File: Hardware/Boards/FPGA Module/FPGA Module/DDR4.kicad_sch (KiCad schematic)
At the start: 39 parts, among them U17 MT40A512M16LY-075:E, U9 TPS74801AWDRC

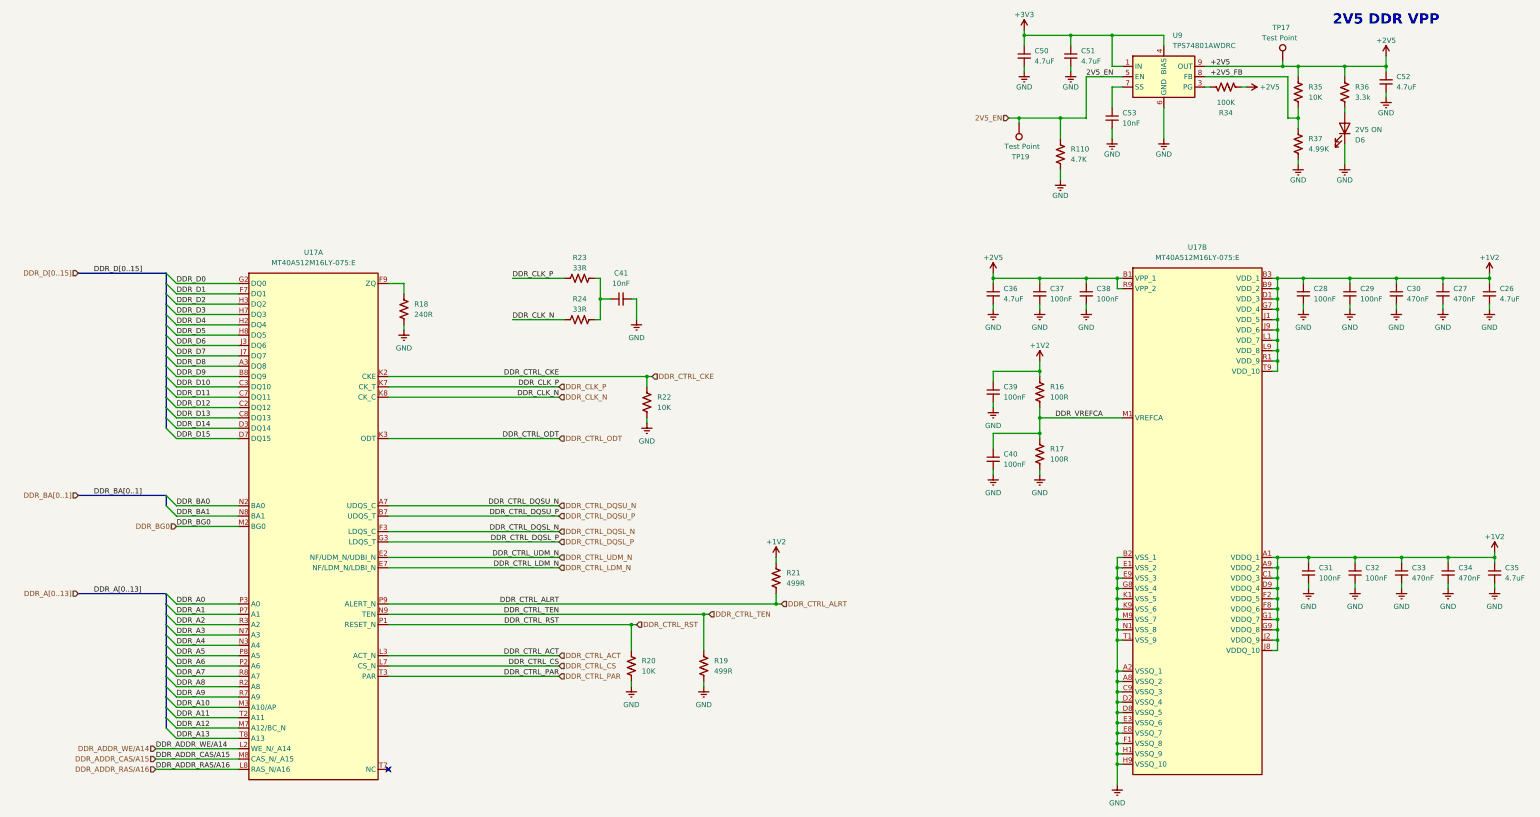
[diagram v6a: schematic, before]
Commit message: Completed FPGA module PCB layout
Started PCB routing
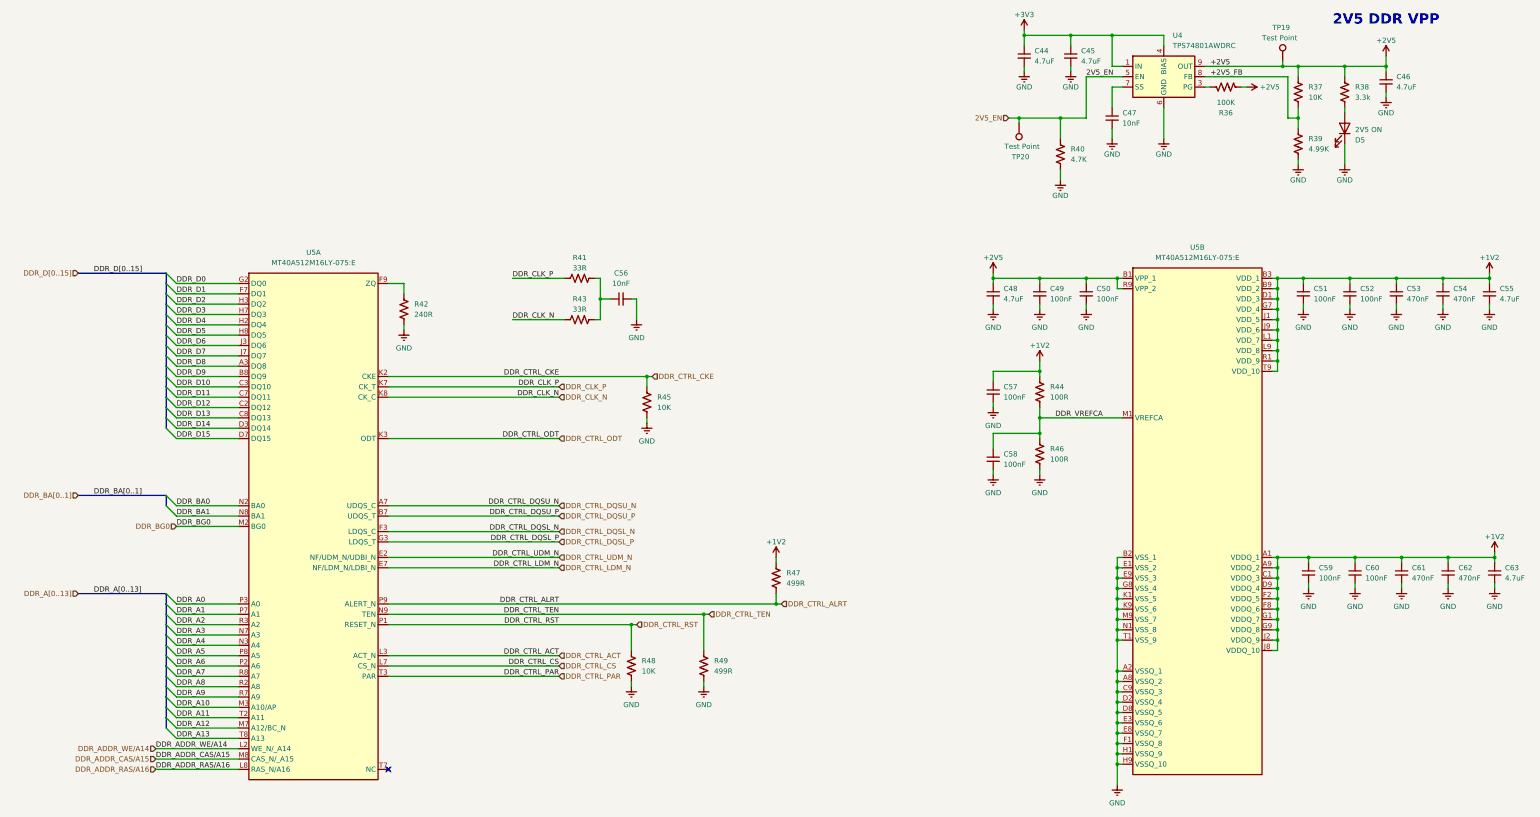
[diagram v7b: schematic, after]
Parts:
- C47: renamed from C53; footprint Capacitor_SMD:C_0402_1005Metric -> Capacitor_SMD:C_0201_0603Metric
- C49: renamed from C37; footprint Capacitor_SMD:C_0402_1005Metric -> Capacitor_SMD:C_0201_0603Metric
- C50: renamed from C38; footprint Capacitor_SMD:C_0402_1005Metric -> Capacitor_SMD:C_0201_0603Metric
- C51: renamed from C28; footprint Capacitor_SMD:C_0402_1005Metric -> Capacitor_SMD:C_0201_0603Metric
- C52: renamed from C29; footprint Capacitor_SMD:C_0402_1005Metric -> Capacitor_SMD:C_0201_0603Metric
- C53: renamed from C30; footprint Capacitor_SMD:C_0402_1005Metric -> Capacitor_SMD:C_0201_0603Metric
- C54: renamed from C27; footprint Capacitor_SMD:C_0402_1005Metric -> Capacitor_SMD:C_0201_0603Metric
- C56: renamed from C41; footprint Capacitor_SMD:C_0402_1005Metric -> Capacitor_SMD:C_0201_0603Metric
- C57: renamed from C39; footprint Capacitor_SMD:C_0402_1005Metric -> Capacitor_SMD:C_0201_0603Metric
- C58: renamed from C40; footprint Capacitor_SMD:C_0402_1005Metric -> Capacitor_SMD:C_0201_0603Metric
- C59: renamed from C31; footprint Capacitor_SMD:C_0402_1005Metric -> Capacitor_SMD:C_0201_0603Metric
- C60: renamed from C32; footprint Capacitor_SMD:C_0402_1005Metric -> Capacitor_SMD:C_0201_0603Metric
- C61: renamed from C33; footprint Capacitor_SMD:C_0402_1005Metric -> Capacitor_SMD:C_0201_0603Metric
- C62: renamed from C34; footprint Capacitor_SMD:C_0402_1005Metric -> Capacitor_SMD:C_0201_0603Metric
- R36: renamed from R34; footprint Resistor_SMD:R_0402_1005Metric -> Resistor_SMD:R_0201_0603Metric
- R37: renamed from R35; footprint Resistor_SMD:R_0402_1005Metric -> Resistor_SMD:R_0201_0603Metric
- R38: renamed from R36; footprint Resistor_SMD:R_0402_1005Metric -> Resistor_SMD:R_0201_0603Metric
- R39: renamed from R37; footprint Resistor_SMD:R_0402_1005Metric -> Resistor_SMD:R_0201_0603Metric
- R40: renamed from R110; footprint Resistor_SMD:R_0402_1005Metric -> Resistor_SMD:R_0201_0603Metric
- R41: renamed from R23; footprint Resistor_SMD:R_0402_1005Metric -> Resistor_SMD:R_0201_0603Metric
- R42: renamed from R18; footprint Resistor_SMD:R_0402_1005Metric -> Resistor_SMD:R_0201_0603Metric
- R43: renamed from R24; footprint Resistor_SMD:R_0402_1005Metric -> Resistor_SMD:R_0201_0603Metric
- R44: renamed from R16; footprint Resistor_SMD:R_0402_1005Metric -> Resistor_SMD:R_0201_0603Metric
- R45: renamed from R22; footprint Resistor_SMD:R_0402_1005Metric -> Resistor_SMD:R_0201_0603Metric
- R46: renamed from R17; footprint Resistor_SMD:R_0402_1005Metric -> Resistor_SMD:R_0201_0603Metric
- R47: renamed from R21; footprint Resistor_SMD:R_0402_1005Metric -> Resistor_SMD:R_0201_0603Metric
- R48: renamed from R20; footprint Resistor_SMD:R_0402_1005Metric -> Resistor_SMD:R_0201_0603Metric
- R49: renamed from R19; footprint Resistor_SMD:R_0402_1005Metric -> Resistor_SMD:R_0201_0603Metric
- renumbered C50 to C44, C51 to C45, C52 to C46, C36 to C48, C26 to C55, C35 to C63, D6 to D5, TP17 to TP19, TP19 to TP20, U9 to U4, U17 to U5

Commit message: Updated SCH and Layout
Added temp sensors for DCDC's, Added MCU control for FPGA mode, removed mode DIP switch
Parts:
- C44, C45, C46, C48, C55, C63: footprint Capacitor_SMD:C_0402_1005Metric -> Capacitor_SMD:C_0201_0603Metric
- R39: value 4.99K -> 5.1K
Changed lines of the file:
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@@
 			)
 		)
-		(property "Footprint" "Capacitor_SMD:C_0402_1005Metric"
+		(property "Footprint" "Capacitor_SMD:C_0201_0603Metric"
 			(at 270.51 38.1 0)
 			(effects
@@
 			)
 		)
-		(property "Footprint" "Capacitor_SMD:C_0402_1005Metric"
+		(property "Footprint" "Capacitor_SMD:C_0201_0603Metric"
 			(at 386.08 165.1 0)
 			(effects
@@
 			)
 		)
-		(property "Footprint" "Capacitor_SMD:C_0402_1005Metric"
+		(property "Footprint" "Capacitor_SMD:C_0201_0603Metric"
 			(at 359.41 44.45 0)
 			(effects
@@
 			)
 		)
-		(property "Footprint" "Capacitor_SMD:C_0402_1005Metric"
+		(property "Footprint" "Capacitor_SMD:C_0201_0603Metric"
 			(at 262.89 96.52 0)
 			(effects
@@
 			)
 		)
-		(property "Footprint" "Capacitor_SMD:C_0402_1005Metric"
+		(property "Footprint" "Capacitor_SMD:C_0201_0603Metric"
 			(at 281.94 38.1 0)
 			(effects
@@
 			)
 		)
-		(property "Value" "4.99K"
+		(property "Value" "5.1K"
 			(at 340.36 60.9599 0)
 			(effects
@@
 			)
 		)
-		(property "Footprint" "Capacitor_SMD:C_0402_1005Metric"
+		(property "Footprint" "Capacitor_SMD:C_0201_0603Metric"
 			(at 384.81 96.52 0)
 			(effects
